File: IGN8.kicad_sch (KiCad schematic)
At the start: 43 parts, among them Q1 ISL9V3040D3ST, Q2 ISL9V3040D3ST, Q3 ISL9V3040D3ST, Q4 ISL9V3040D3ST, Q5 ISL9V3040D3ST, Q6 ISL9V3040D3ST, Q7 ISL9V3040D3ST, Q8 ISL9V3040D3ST, U5 SN74LVC4245APWR

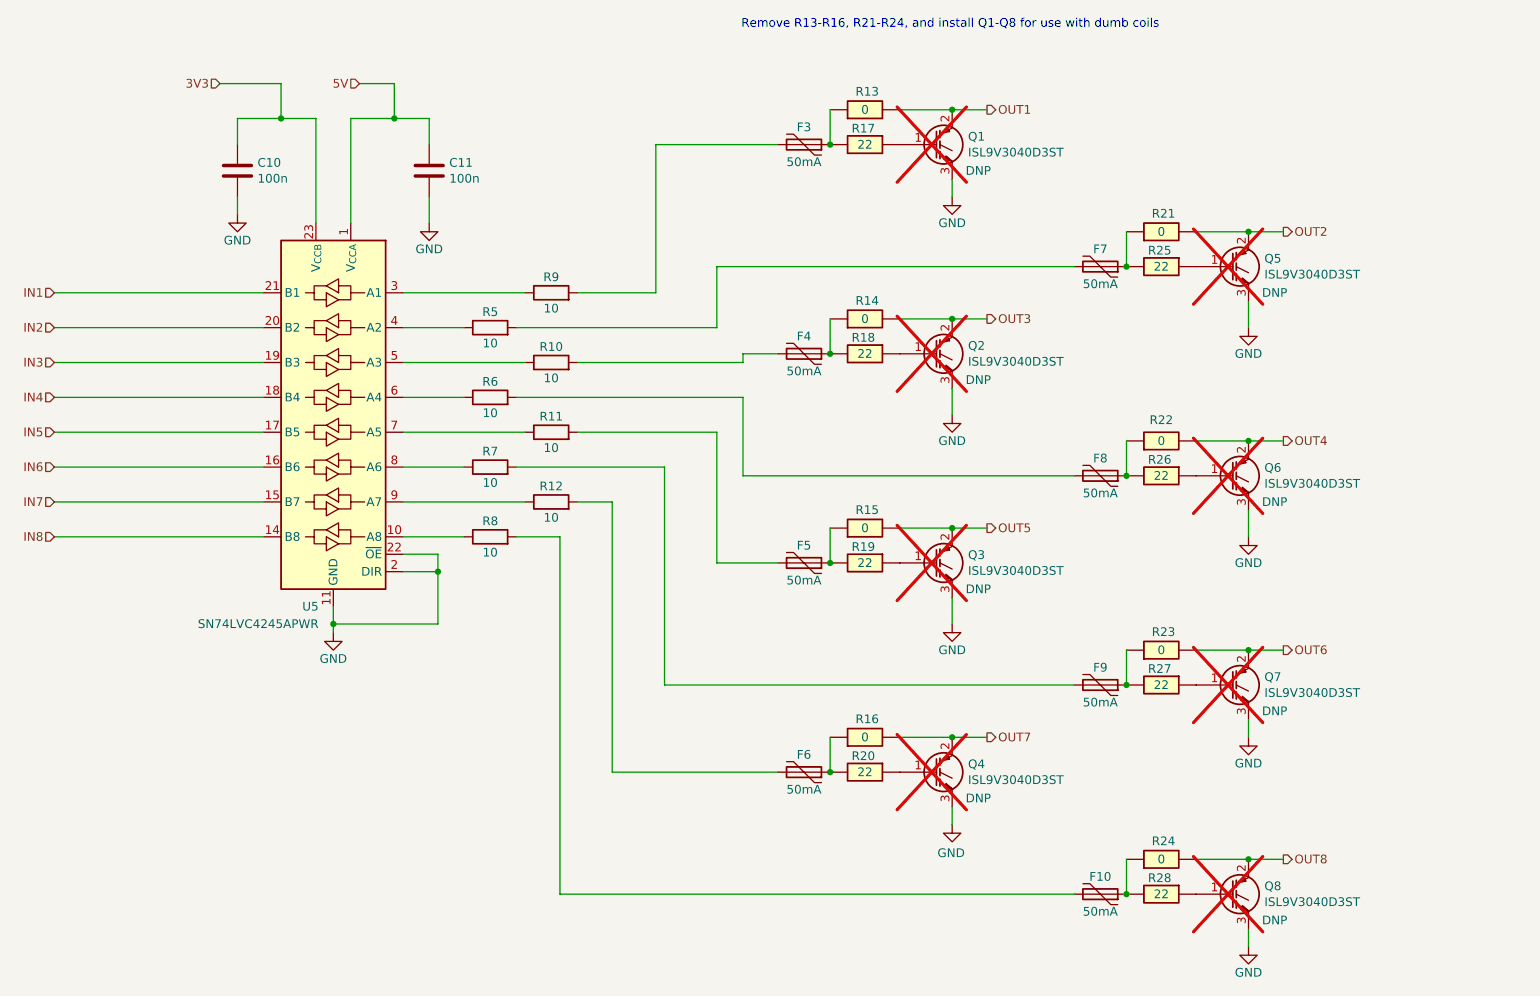
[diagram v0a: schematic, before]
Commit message: Standalone version without hellen-one
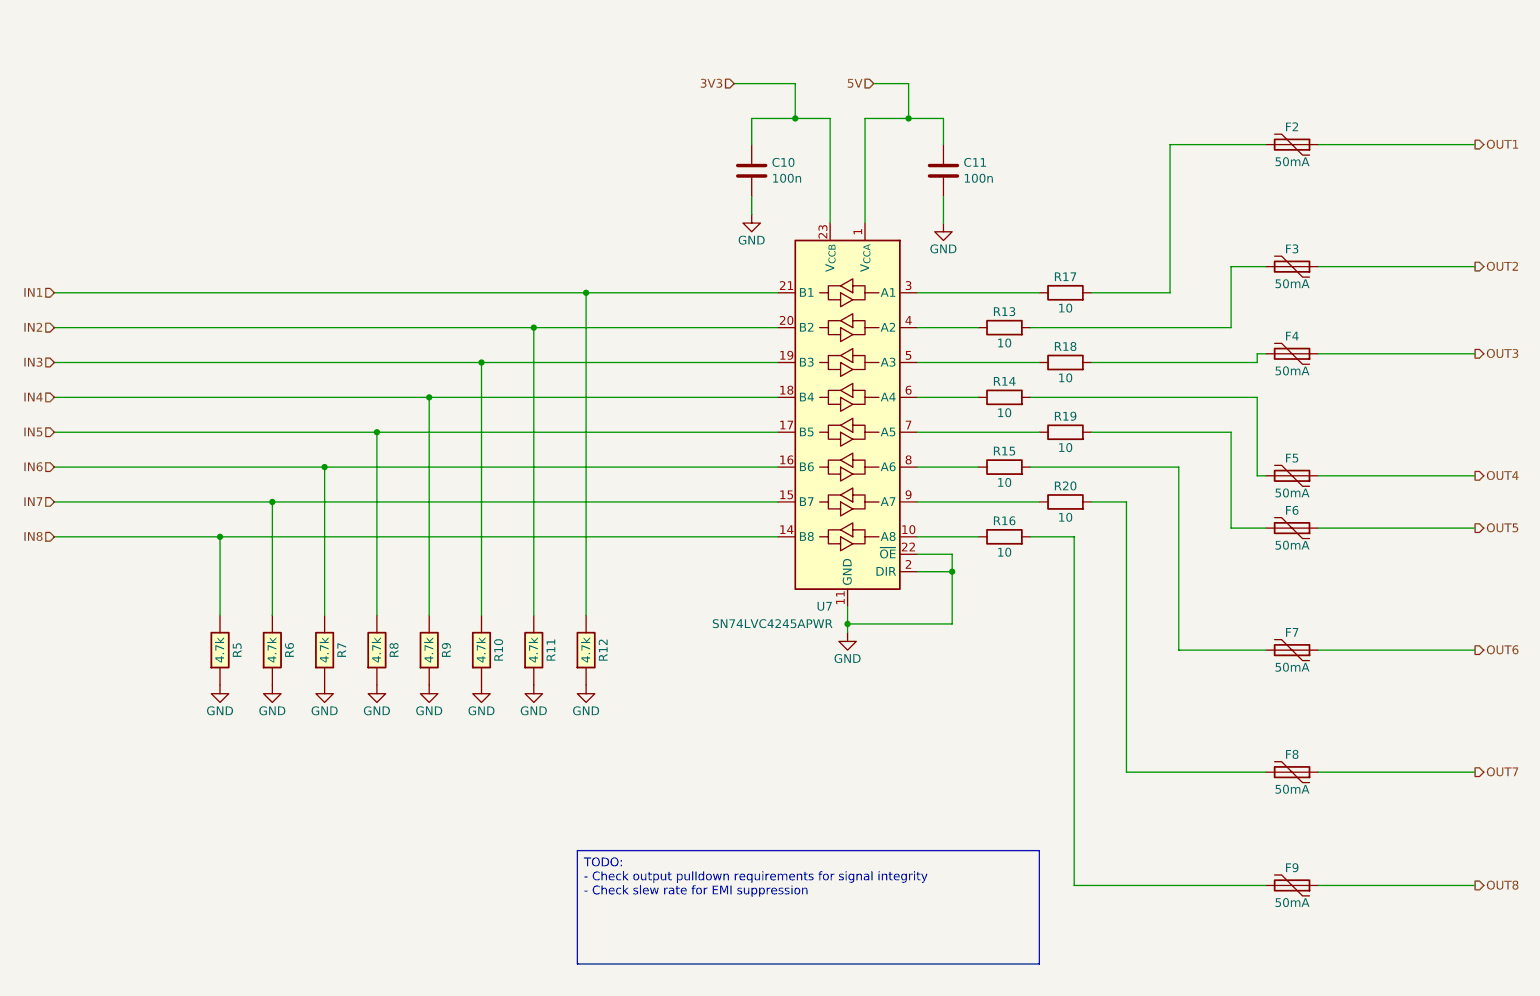
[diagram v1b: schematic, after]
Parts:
- removed Q1, Q2, Q3, Q4, Q5, Q6, Q7, Q8: ISL9V3040D3ST, Package_TO_SOT_SMD:TO-252-2, symbol Device:Q_NIGBT_GCE
- removed R13, R14, R15, R16, R21, R22, R23, R24: 0, Resistor_SMD:R_1206_3216Metric, symbol hellen-one-common:Res
- removed R17, R18, R19, R20, R25, R26, R27, R28: 22, hellen-one-common:R0603, symbol hellen-one-common:Res
- added R10, R11, R12, R5, R6, R7, R8, R9: 4.7k, Resistor_SMD:R_0603_1608Metric, symbol hellen-one-common:Res
- renumbered F3 to F2, F7 to F3, F8 to F5, F5 to F6, F9 to F7, F6 to F8, F10 to F9, R5 to R13, R6 to R14, R7 to R15, R8 to R16, R9 to R17, R10 to R18, R11 to R19, R12 to R20, U5 to U7
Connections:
- net GND: now also R10.1, R11.1, R12.1, R5.1, R6.1, R7.1, R8.1, R9.1
- net IN1: now also R12.2
- net IN2: now also R11.2
- net IN3: now also R10.2
- net IN4: now also R9.2
- net IN5: now also R8.2
- net IN6: now also R7.2
- net IN7: now also R6.2
- net IN8: now also R5.2
- net OUT1: now also F2.1
- net OUT2: now also F3.1
- net OUT3: now also F4.1
- net OUT4: now also F5.1
- net OUT5: now also F6.1
- net OUT6: now also F7.1
- net OUT7: now also F8.1
- net OUT8: now also F9.1
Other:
- note removed: "Remove R13-R16, R21-R24, and install Q1-Q8 for use with dumb coils"
- moved on the sheet: C10, C11, F2, F3, F4, F5, F6, F7, F8, F9, R13, R14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
